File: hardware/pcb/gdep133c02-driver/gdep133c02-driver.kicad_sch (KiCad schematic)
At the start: 0 parts

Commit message: save
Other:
- sheet Host isolation and test points renamed Host interface and test points
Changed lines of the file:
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@@
-(kicad_sch
-	(version 20260306)
-	(generator "eeschema")
-	(generator_version "10.0")
-	(paper "A4")
-	(title_block
-		(title "GDEP133C02 minimum driver - DRAFT")
-		(date "2026-10-01")
-		(rev "0.1")
-		(company "album")
-	)
-	(sheet
-		(at 35 105)
-		(size 90 20)
-		(exclude_from_sim no)
-		(in_bom yes)
-		(on_board yes)
-		(dnp no)
-		(stroke
-			(width 0)
-			(type solid)
-		)
-		(fill
-			(color 0 0 0 0)
-		)
-		(property "Sheetname" "Host isolation and test points"
-			(at 35 104 0)
-			(show_name no)
-			(do_not_autoplace no)
-			(effects
-				(font
-					(size 1.27 1.27)
-				)
-				(justify left bottom)
-			)
-		)
-		(property "Sheetfile" "interface.kicad_sch"
-			(at 35 126 0)
-			(show_name no)
-			(do_not_autoplace no)
-			(effects
-				(font
-					(size 1.27 1.27)
-				)
-				(justify left top)
-			)
-		)
-		(instances
-			(project "gdep133c02-driver"
-				(path "/2df5ab9d-628b-53bd-a709-8806893b789a"
-					(page "4")
-				)
-			)
-		)
-	)
-	(sheet
-		(at 35 35)
-		(size 90 20)
-		(exclude_from_sim no)
-		(in_bom yes)
-		(on_board yes)
-		(dnp no)
-		(stroke
-			(width 0)
-			(type solid)
-		)
-		(fill
-			(color 0 0 0 0)
-		)
-		(property "Sheetname" "Power converters"
-			(at 35 34 0)
-			(show_name no)
-			(do_not_autoplace no)
-			(effects
-				(font
-					(size 1.27 1.27)
-				)
-				(justify left bottom)
-			)
-		)
-		(property "Sheetfile" "power.kicad_sch"
-			(at 35 56 0)
-			(show_name no)
-			(do_not_autoplace no)
-			(effects
-				(font
-					(size 1.27 1.27)
-				)
-				(justify left top)
-			)
-		)
-		(instances
-			(project "gdep133c02-driver"
-				(path "/2df5ab9d-628b-53bd-a709-8806893b789a"
-					(page "2")
-				)
-			)
-		)
-	)
-	(sheet
-		(at 35 70)
-		(size 90 20)
-		(exclude_from_sim no)
-		(in_bom yes)
-		(on_board yes)
-		(dnp no)
-		(stroke
-			(width 0)
-			(type solid)
-		)
-		(fill
-			(color 0 0 0 0)
-		)
-		(property "Sheetname" "Panel and temperature"
-			(at 35 69 0)
-			(show_name no)
-			(do_not_autoplace no)
-			(effects
-				(font
-					(size 1.27 1.27)
-				)
-				(justify left bottom)
-			)
-		)
-		(property "Sheetfile" "panel.kicad_sch"
-			(at 35 91 0)
-			(show_name no)
-			(do_not_autoplace no)
-			(effects
-				(font
-					(size 1.27 1.27)
-				)
-				(justify left top)
-			)
-		)
-		(instances
-			(project "gdep133c02-driver"
-				(path "/2df5ab9d-628b-53bd-a709-8806893b789a"
-					(page "3")
-				)
-			)
-		)
-	)
-	(sheet_instances
-		(path "/"
-			(page "1")
-		)
-	)
-	(embedded_fonts no)
-)

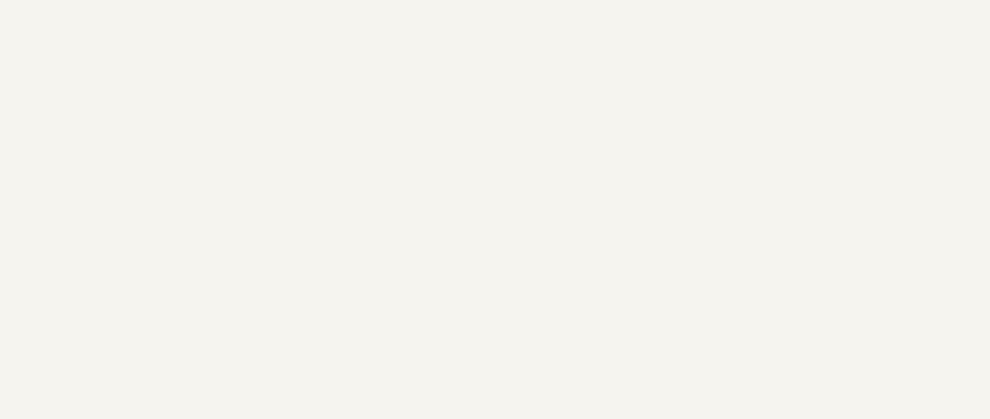
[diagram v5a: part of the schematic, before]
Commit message: feat(pcb): adopt 17 basic-library groups and release v0.11 prototype
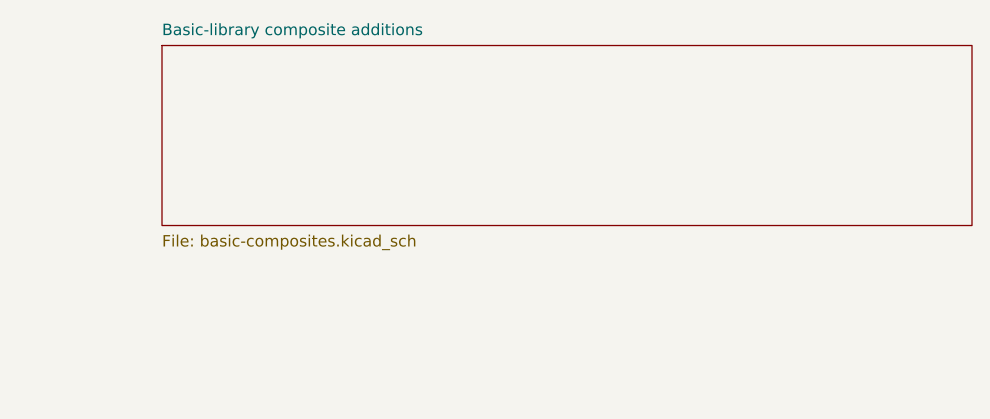
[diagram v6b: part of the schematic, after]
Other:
- added sheet Basic-library composite additions (basic-composites.kicad_sch)
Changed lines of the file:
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@@
-(kicad_sch
-	(version 20260306)
-	(generator "eeschema")
-	(generator_version "10.0")
-	(paper "A4")
-	(title_block
-		(title "GDEP133C02 minimum driver - DRAFT")
-		(date "2026-10-09")
-		(rev "0.10-E01")
-		(company "album")
-	)
-	(sheet
-		(at 35 105)
-		(size 90 20)
-		(exclude_from_sim no)
-		(in_bom yes)
-		(on_board yes)
-		(dnp no)
-		(stroke
-			(width 0)
-			(type solid)
-		)
-		(fill
-			(color 0 0 0 0)
-		)
-		(property "Sheetname" "Host interface and test points"
-			(at 35 104 0)
-			(show_name no)
-			(do_not_autoplace no)
-			(effects
-				(font
-					(size 1.27 1.27)
-				)
-				(justify left bottom)
-			)
-		)
-		(property "Sheetfile" "interface.kicad_sch"
-			(at 35 126 0)
-			(show_name no)
-			(do_not_autoplace no)
-			(effects
-				(font
-					(size 1.27 1.27)
-				)
-				(justify left top)
-			)
-		)
-		(instances
-			(project "gdep133c02-driver"
-				(path "/2df5ab9d-628b-53bd-a709-8806893b789a"
-					(page "4")
-				)
-			)
-		)
-	)
-	(sheet
-		(at 35 35)
-		(size 90 20)
-		(exclude_from_sim no)
-		(in_bom yes)
-		(on_board yes)
-		(dnp no)
-		(stroke
-			(width 0)
-			(type solid)
-		)
-		(fill
-			(color 0 0 0 0)
-		)
-		(property "Sheetname" "Power converters"
-			(at 35 34 0)
-			(show_name no)
-			(do_not_autoplace no)
-			(effects
-				(font
-					(size 1.27 1.27)
-				)
-				(justify left bottom)
-			)
-		)
-		(property "Sheetfile" "power.kicad_sch"
-			(at 35 56 0)
-			(show_name no)
-			(do_not_autoplace no)
-			(effects
-				(font
-					(size 1.27 1.27)
-				)
-				(justify left top)
-			)
-		)
-		(instances
-			(project "gdep133c02-driver"
-				(path "/2df5ab9d-628b-53bd-a709-8806893b789a"
-					(page "2")
-				)
-			)
-		)
-	)
-	(sheet
-		(at 35 70)
-		(size 90 20)
-		(exclude_from_sim no)
-		(in_bom yes)
-		(on_board yes)
-		(dnp no)
-		(stroke
-			(width 0)
-			(type solid)
-		)
-		(fill
-			(color 0 0 0 0)
-		)
-		(property "Sheetname" "Panel and temperature"
-			(at 35 69 0)
-			(show_name no)
-			(do_not_autoplace no)
-			(effects
-				(font
-					(size 1.27 1.27)
-				)
-				(justify left bottom)
-			)
-		)
-		(property "Sheetfile" "panel.kicad_sch"
-			(at 35 91 0)
-			(show_name no)
-			(do_not_autoplace no)
-			(effects
-				(font
-					(size 1.27 1.27)
-				)
-				(justify left top)
-			)
-		)
-		(instances
-			(project "gdep133c02-driver"
-				(path "/2df5ab9d-628b-53bd-a709-8806893b789a"
-					(page "3")
-				)
-			)
-		)
-	)
-	(sheet_instances
-		(path "/"
-			(page "1")
-		)
-	)
-	(embedded_fonts no)
-)
